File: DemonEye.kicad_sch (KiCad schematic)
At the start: 31 parts, among them CN1 PicoBlade 1x06 P1.25mm, Q1 PDTA123EM, Q2 PDTA123EM, Q3 PDTA123EM, Q4 PDTA123EM, Q5 CSD25501F3, U1 WS2814F, U2 TLV76701DRVx, U3 BCR421UFDQ, U4 BCR421UFDQ, U5 BCR421UFDQ, U6 BCR421UFDQ

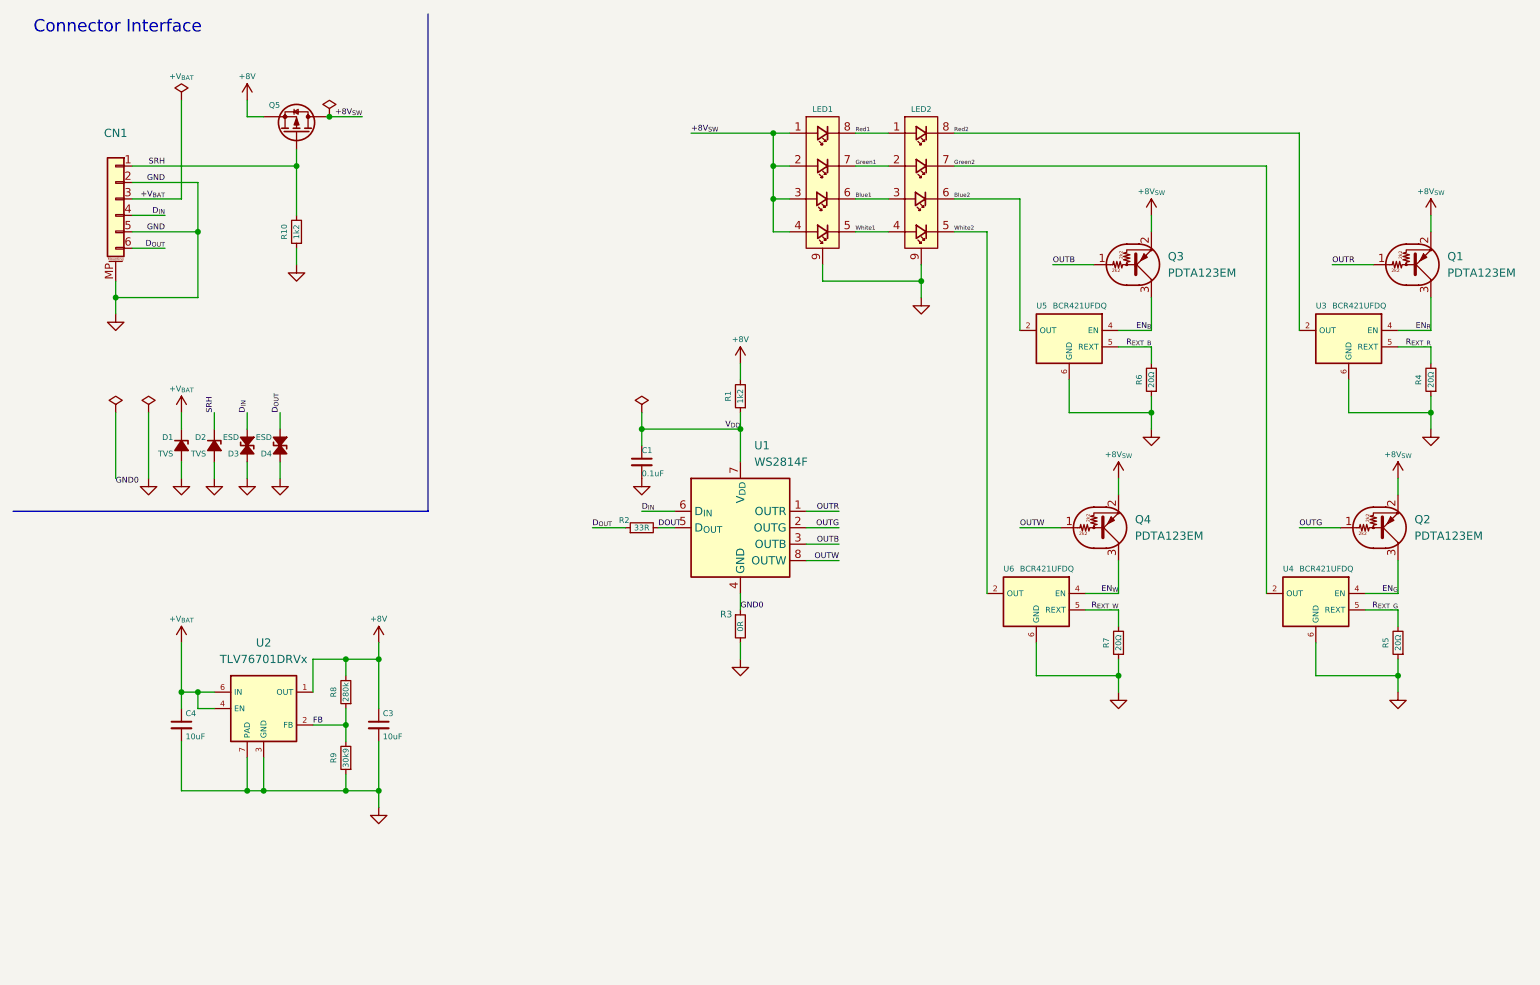
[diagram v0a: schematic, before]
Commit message: Update .gitignore, DemonEye.kicad_pcb, DemonEye.kicad_prl, and 17 more files
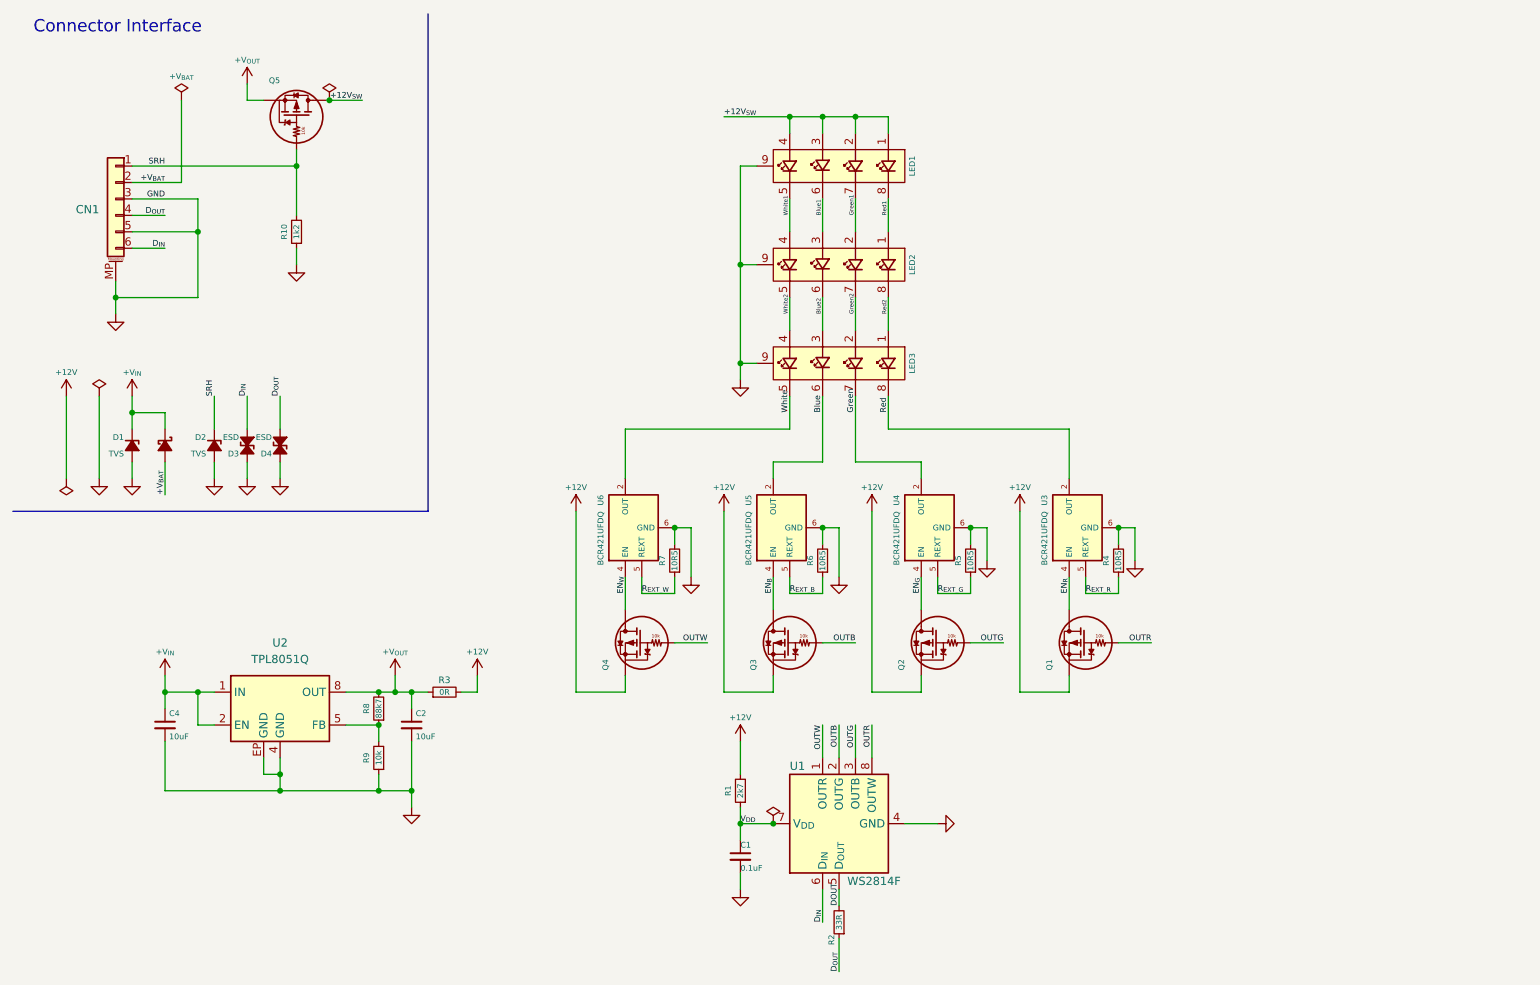
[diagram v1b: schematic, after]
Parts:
- removed C3: 10uF, My Capacitors:C_0603_Dense, symbol Device:C_Small
- removed Q1, Q2, Q3, Q4: PDTA123EM, My Package_Leadless:Diodes_DFN1006-3, symbol PersonalSchematicSymbolLibrary:DTA123E
- removed U2: TLV76701DRVx, My Package_Leadless:WSON-6-1EP_2x2mm_P0.65mm_EP1x1.6mm, symbol My Power Management:TLV76701DRVx
- added C2: 10uF, My Capacitors:C_0805_Nominal, symbol Device:C_Small
- added D5: D_Schottky_Small_Filled, My Package_Leadless:DFN1006-2, symbol PersonalSchematicSymbolLibrary:D_Schottky_Small_Filled
- added LED3: QLSP06RGBXWAJ, Personal_FootprintLibrary:QLSP06RGBXWAJ, symbol PersonalSchematicSymbolLibrary:QLSP06RGBXWAJ
- added Q1, Q2, Q3, Q4: CSD25501F3, My Package_Leadless:Texas_PICOSTAR-YJN_0.7x0.6mm_PicoStar, symbol PersonalSchematicSymbolLibrary:P-Channel_FemtoFET
- added U2: TPL8051Q, Package_DFN_QFN:DFN-8-1EP_3x3mm_P0.65mm_EP1.55x2.4mm, symbol My Power DCDC:TPL8051Q
- C4: footprint My Capacitors:C_0603_Dense -> My Capacitors:C_0805_Nominal; Distributor Link 1 https://www.digikey.com/en/products/detail/murata-electronics/GRM188R6YA106MA73D/5877411 -> https://www.digikey.com/en/products/detail/murata-electronics/GCM21BC71E106KE36L/16821116; Distributor Link 2 https://www.mouser.com/ProductDetail/Murata-Electronics/GRM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 -> https://www.mouser.com/en/ProductDetail/Murata-Electronics/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; LCSC C194427 -> C5367383; Manufacturer Part Number GRM188R6YA106MA73D -> GCM21BC71E106KE36L
- Q5: footprint My Package_Leadless:Texas_-YJN_0.7x0.6mm_PicoStar -> My Package_Leadless:Texas_PICOSTAR-YJN_0.7x0.6mm_PicoStar; symbol PersonalSchematicSymbolLibrary:Q_PMOS -> PersonalSchematicSymbolLibrary:P-Channel_FemtoFET
- R1: value 1k2 -> 2k7; Distributor Link 1 https://www.digikey.com/en/products/detail/yageo/AC0201FR-071K2L/5894355 -> https://www.digikey.com/en/products/detail/yageo/AC0201FR-072K7L/5894506; Distributor Link 2 https://www.mouser.com/ProductDetail/YAGEO/AC0201FR-071K2L?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 -> https://www.mouser.com/en/ProductDetail/YAGEO/AC0201FR-072K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; LCSC C226448 -> C226497; Manufacturer Part Number AC0201FR-071K2L -> AC0201FR-072K7L
- R10: footprint My Resistors:R_0201_Dense -> My Resistors:R_0402_Nominal; Distributor Link 1 https://www.digikey.com/en/products/detail/yageo/AC0201FR-0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 -> https://www.digikey.com/en/products/detail/yageo/AC0402FR-0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; Distributor Link 2 https://www.mouser.com/ProductDetail/YAGEO/AC0201FR-071K2L?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 -> https://www.mouser.com/en/ProductDetail/YAGEO/AC0402FR-071K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; LCSC C226448 -> C144793; Manufacturer Part Number AC0201FR-071K2L -> AC0402FR-071K2L
- R2: footprint My Resistors:R_0201_Dense -> My Resistors:R_0402_Nominal; Distributor Link 1 https://www.digikey.com/en/products/detail/yageo/AC0201FR-0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 -> https://www.digikey.com/en/products/detail/yageo/AC0402FR-0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; Distributor Link 2 https://www.mouser.com/ProductDetail/YAGEO/AC0201FR-0733RL?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 -> https://www.mouser.com/en/ProductDetail/YAGEO/AC0402FR-0733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; LCSC C226514 -> C227000; Manufacturer Part Number AC0201FR-0733RL -> AC0402FR-0733RL
- R3: footprint My Resistors:R_0402_Nominal -> My Resistors:R_0603_Nominal; Distributor Link 1 https://www.digikey.com/en/products/detail/yageo/AC0402FR-0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 -> https://www.digikey.com/en/products/detail/yageo/AC0603FR-0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; Distributor Link 2 https://www.mouser.com/ProductDetail/YAGEO/AC0402FR-070RL?q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 -> https://www.mouser.com/en/ProductDetail/YAGEO/AC0603FR-070R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; LCSC C226739 -> C116699; Manufacturer Part Number AC0402FR-070RL -> AC0603FR-070RL
- R4, R5, R6, R7: value 20Ω -> 10R5; Distributor Link 1 https://www.digikey.com/en/products/detail/yageo/AC0201FR-0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 -> (none); Distributor Link 2 https://www.mouser.com/ProductDetail/YAGEO/AC0201FR-0720RL?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 -> https://www.mouser.com/en/ProductDetail/Royalohm/0201WMF105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; LCSC C226464 -> C784112; MPN (none) -> 0201WMF105JTEE; Manufacturer YAGEO -> UNI-ROYAL(Uniroyal Elec); Manufacturer Part Number AC0201FR-0720RL -> (none)
- R8: value 280k -> 88k7; Distributor Link 2 https://www.mouser.com/ProductDetail/Royalohm/0201WMF2803TE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 -> https://www.mouser.com/en/ProductDetail/Royalohm/0201WMF887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; LCSC C778392 -> C423412; Manufacturer Part Number 0201WMF2803TEE -> 0201WMF8872TEE
- R9: value 30k9 -> 10k; Distributor Link 1 (none) -> https://www.digikey.com/en/products/detail/yageo/AC0201FR-0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; Distributor Link 2 https://www.mouser.com/ProductDetail/Royalohm/0201WMF3092TE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 -> https://www.mouser.com/en/ProductDetail/YAGEO/AC0201FR-0710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; LCSC C473585 -> C144833; Manufacturer UNI-ROYAL(Uniroyal Elec) -> YAGEO; Manufacturer Part Number 0201WMF3092TEE -> AC0201FR-0710KL
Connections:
- net +V_{BAT}: now also CN1.2 (Pin_2), D5.2 (A); no longer C4.1, CN1.3 (Pin_3), D1.1 (K)
- net Blue2: now also LED3.3 (Blue_A); no longer U5.2 (OUT)
- net D_{IN}: now also CN1.6 (Pin_4); no longer CN1.4 (Pin_4)
- net D_{OUT}: now also CN1.4 (Pin_4); no longer CN1.6 (Pin_4)
- net EN_{B}: now also Q3.3 (D)
- net EN_{G}: now also Q2.3 (D)
- net EN_{R}: now also Q1.3 (D)
- net EN_{W}: now also Q4.3 (D)
- net GND: now also CN1.3 (Pin_3), R4.2, R5.2, R6.2, R7.2, U1.4 (GND), C2.2, LED3.9 (EP), U2.4 (GND), U2.EP (GND); no longer CN1.2 (Pin_2), R3.2, R4.1, R5.1, R6.1, R7.1
- net Green2: now also LED3.2 (Green_A); no longer U4.2 (OUT)
- net OUTB: now also U1.2 (OUTG), Q3.1 (G); no longer U1.3 (OUTB)
- net OUTG: now also U1.3 (OUTB), Q2.1 (G); no longer U1.2 (OUTG)
- net OUTR: now also U1.8 (OUTW), Q1.1 (G); no longer U1.1 (OUTR)
- net OUTW: now also U1.1 (OUTR), Q4.1 (G); no longer U1.8 (OUTW)
- net R_{EXT_B}: now also R6.1; no longer R6.2
- net R_{EXT_G}: now also R5.1; no longer R5.2
- net R_{EXT_R}: now also R4.1; no longer R4.2
- net R_{EXT_W}: now also R7.1; no longer R7.2
- net Red2: now also LED3.1 (Red_A); no longer U3.2 (OUT)
- net White2: now also LED3.4 (White_A); no longer U6.2 (OUT)
- net +8V renamed +V_{OUT}
- net +V_{OUT}: now also R3.1, C2.1, U2.8 (OUT); no longer R1.2
- net +8V_{SW} renamed +12V_{SW}
- net FB: no longer names the net of R8.1, R9.2
- net FB: now also U2.5 (FB)
- removed net GND0: R3.1, U1.4 (GND)
- new net: U2.3 (NC), U2.6 (NC)
- new net +12V: Q1.2 (S), Q2.2 (S), Q3.2 (S), Q4.2 (S), R1.2, R3.2
- new net +V_{IN}: C4.1, D1.1 (K), D5.1 (K), U2.1 (IN), U2.2 (EN)
- new net Blue: LED3.6 (Blue_K), U5.2 (OUT)
- new net Green: LED3.7 (Green_K), U4.2 (OUT)
- new net Red: LED3.8 (Red_K), U3.2 (OUT)
- new net White: LED3.5 (White_K), U6.2 (OUT)
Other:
- moved on the sheet: C1, C4, D1, LED1, LED2, R1, R2, R3, R7, U1, U3, U4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

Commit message: reworked the protection circuitry for the SRH signal to protect the PFET from surges and >16V load dumps
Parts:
- added D6: 16V, My Package_Leadless:DFN1006-2, symbol PersonalSchematicSymbolLibrary:D_Zener_Small_Filled
- added R11: 200R, My Resistors:R_0402_Nominal, symbol Device:R_Small
- R10: value 1k2 -> 10k; footprint My Resistors:R_0402_Nominal -> My Resistors:R_0201_Nominal; Distributor Link 1 https://www.digikey.com/en/products/detail/yageo/AC0402FR-0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 -> https://www.digikey.com/en/products/detail/yageo/AC0201FR-0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; Distributor Link 2 https://www.mouser.com/en/ProductDetail/YAGEO/AC0402FR-071K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 -> https://www.mouser.com/en/ProductDetail/YAGEO/AC0201FR-0710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; LCSC C144793 -> C144833; Manufacturer Part Number AC0402FR-071K2L -> AC0201FR-0710KL
- R4, R5, R6, R7: value 10R5 -> 10R; Distributor Link 1 (none) -> https://www.digikey.com/en/products/detail/yageo/AF0201FR-0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; Distributor Link 2 https://www.mouser.com/en/ProductDetail/Royalohm/0201WMF105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 -> https://www.mouser.com/en/ProductDetail/YAGEO/AF0201FR-0710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; LCSC C784112 -> C143979; MPN 0201WMF105JTEE -> AF0201FR-0710RL; Manufacturer UNI-ROYAL(Uniroyal Elec) -> YAGEO
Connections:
- net GND: now also D6.2 (A)
- net SRH: now also R11.2; no longer Q5.1 (G), R10.2
- new net SRH_{G}: D6.1 (K), Q5.1 (G), R10.2, R11.1
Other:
- moved on the sheet: R10
